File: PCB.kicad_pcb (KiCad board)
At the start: 2 copper layers, 13 parts, among them SW1 RotaryEncoder_Switch, U2 MOUDLE-SEEEDUINO-XIAO

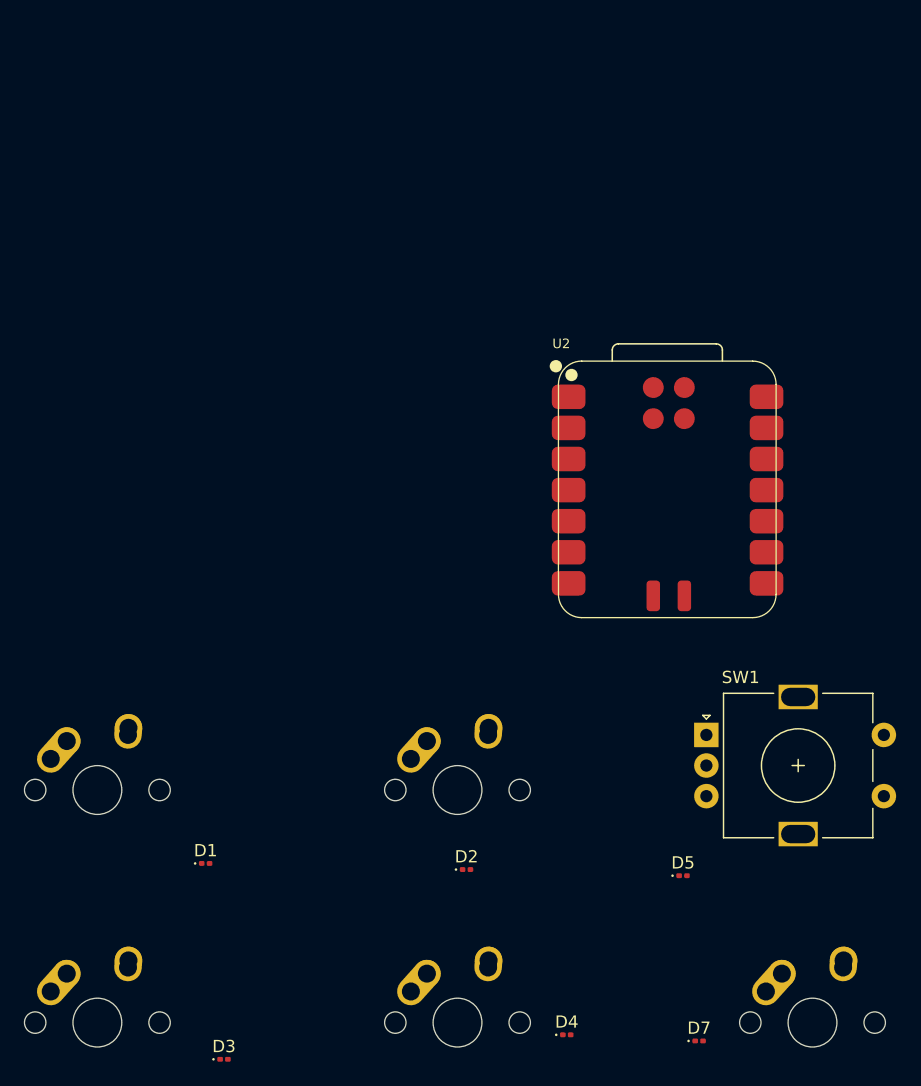
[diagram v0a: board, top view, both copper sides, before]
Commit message: update to pcb and schematic
made with following the guide. will change to make my own
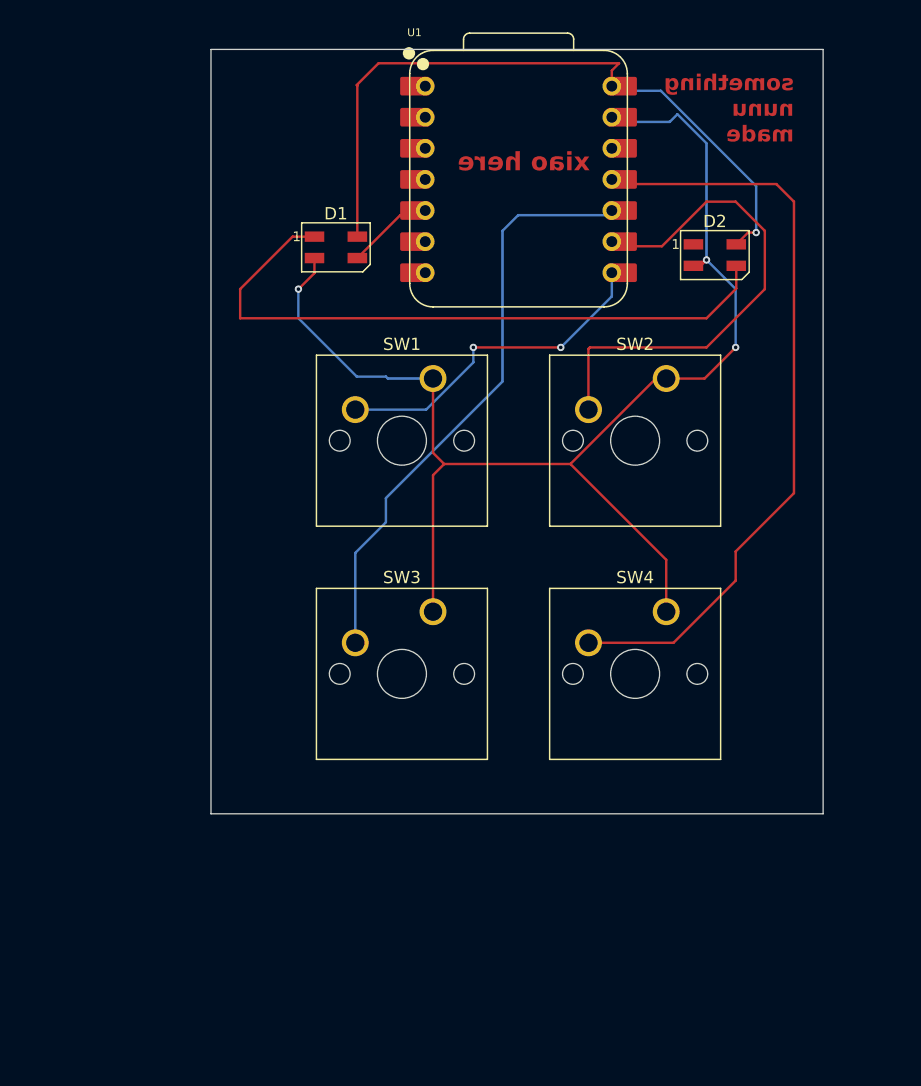
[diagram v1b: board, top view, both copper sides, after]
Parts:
- removed D3, D4, D5, D7: D_Small, Diode_SMD:D_0201_0603Metric
- removed MX1, MX2, MX3, MX4, MX9: MX-NoLED, MX_Alps_Hybrid:MX-1.5U-NoLED
- removed U2: MOUDLE-SEEEDUINO-XIAO, Seeed Studio XIAO Series Library:XIAO-RP2040-SMD
- added SW2: SW_Push, Button_Switch_Keyboard:SW_Cherry_MX_1.00u_PCB, F.Cu at (192.0, 85.9)
- added SW3: SW_Push, Button_Switch_Keyboard:SW_Cherry_MX_1.00u_PCB, F.Cu at (172.9, 104.9)
- added SW4: SW_Push, Button_Switch_Keyboard:SW_Cherry_MX_1.00u_PCB, F.Cu at (192.0, 104.9)
- added U1: XIAO-RP2040-DIP, Seeed Studio XIAO Series Library:XIAO-RP2040-DIP, F.Cu at (179.9, 69.6)
- D1, D2: value D_Small -> SK6812MINI; footprint Diode_SMD:D_0201_0603Metric -> LED_SMD:LED_SK6812MINI_PLCC4_3.5x3.5mm_P1.75mm
- SW1: value RotaryEncoder_Switch -> SW_Push; footprint Rotary_Encoder:RotaryEncoder_Alps_EC11E-Switch_Vertical_H20mm -> Button_Switch_Keyboard:SW_Cherry_MX_1.00u_PCB
- moved D2 54.1 mm to (195.9, 75.8)
- moved D1 51.4 mm to (165.0, 75.2)
- moved SW1 36.7 mm to (172.9, 85.9)
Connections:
- D1 pad 1: ROW0 -> Net-(D1-DOUT)
- D1 pad 2: Net-(D1-A) -> GND
- D2 pad 1: ROW0 -> unconnected-(D2-DOUT-Pad1)
- D2 pad 2: Net-(D2-A) -> GND
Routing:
- net GND: track 0.00 -> 109.3 mm, vias 0 -> 3
- net Net-(U1-GPIO3/MOSI): track 0.00 -> 62.5 mm
- net +5V: track 0.00 -> 57.9 mm, vias 0 -> 1
- net Net-(D1-DOUT): track 0.00 -> 53.6 mm
- net Net-(U1-GPIO4/MISO): track 0.00 -> 48.1 mm
- net Net-(U1-GPIO2/SCK): track 0.00 -> 40.7 mm
- net Net-(U1-GPIO1/RX): track 0.00 -> 27.1 mm, vias 0 -> 2
- net Net-(D1-DIN): track 0.00 -> 7.00 mm
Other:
- board outline added: 50 x 62.4 mm
- board text added: "something nunu made"
- board text added: "xiao here"
